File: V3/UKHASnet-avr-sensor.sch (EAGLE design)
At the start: 25 parts, among them J1 AVR_SPI_PRG_62X3_LOCK, U1 MCP1700-3302E/TO, U2 ATMEGA328P-PU, X2 SMA-142-0711-821/826, Y1 RESONATORPTH

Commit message: Add final V3 files.
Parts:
- removed JP1: M02PTH, SparkFun-Connectors:M02PTH
- added JP7: M02JST-PTH-VERT, SparkFun-Connectors:M02JST-PTH-VERT
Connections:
- net GND: now also JP6.1, JP6.2, JP7.1; no longer JP1.1, JP6.3, JP6.4
- net SENSE1: now also JP6.3; no longer JP6.2
- net SENSE_VCC: now also JP6.4; no longer JP6.1
- net VIN: now also JP7.2; no longer JP1.2
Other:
- moved on the sheet: JP6
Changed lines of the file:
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@@
 <part name="U$1" library="hopeRF2" deviceset="RFM69HW" device=""/>
 <part name="J1" library="SparkFun-Connectors" deviceset="AVR_SPI_PRG_6" device="2X3_LOCK"/>
-<part name="JP1" library="SparkFun-Connectors" deviceset="M02" device="PTH"/>
 <part name="JP2" library="SparkFun-Connectors" deviceset="M01" device="PTH"/>
 <part name="JP3" library="SparkFun-Connectors" deviceset="M01" device="PTH"/>
@@
 <part name="X2" library="con-coax" deviceset="SMA-" device="142-0711-821/826"/>
 <part name="JP6" library="SparkFun-Connectors" deviceset="M04" device="PTH"/>
+<part name="JP7" library="SparkFun-Connectors" deviceset="M02" device="JST-PTH-VERT"/>
 </parts>
 <sheets>
@@
 <instance part="U$1" gate="A" x="25.4" y="-22.86" rot="R180"/>
 <instance part="J1" gate="G$1" x="104.14" y="104.14"/>
-<instance part="JP1" gate="G$1" x="-68.58" y="101.6"/>
 <instance part="JP2" gate="G$1" x="-68.58" y="86.36"/>
 <instance part="JP3" gate="G$1" x="-68.58" y="73.66"/>
@@
 <instance part="JP5" gate="G$1" x="147.32" y="15.24" rot="R180"/>
 <instance part="X2" gate="G1" x="96.52" y="-5.08" rot="MR0"/>
-<instance part="JP6" gate="G$1" x="-33.02" y="55.88" rot="MR180"/>
+<instance part="JP6" gate="G$1" x="-33.02" y="53.34"/>
+<instance part="JP7" gate="G$1" x="-76.2" y="104.14" rot="MR180"/>
 </instances>
 <busses>
@@
 <segment>
 <pinref part="R4" gate="G$1" pin="1"/>
+<wire x1="-17.78" y1="55.88" x2="10.16" y2="55.88" width="0.1524" layer="91"/>
+<label x="0" y="55.88" size="1.778" layer="95"/>
+<pinref part="JP6" gate="G$1" pin="3"/>
 <wire x1="-27.94" y1="55.88" x2="-17.78" y2="55.88" width="0.1524" layer="91"/>
-<wire x1="-17.78" y1="55.88" x2="10.16" y2="55.88" width="0.1524" layer="91"/>
 <junction x="-17.78" y="55.88"/>
-<label x="0" y="55.88" size="1.778" layer="95"/>
-<pinref part="JP6" gate="G$1" pin="2"/>
 </segment>
 </net>
@@
 <wire x1="-55.88" y1="86.36" x2="-53.34" y2="86.36" width="0.1524" layer="91"/>
 <junction x="-55.88" y="86.36"/>
-<pinref part="JP1" gate="G$1" pin="1"/>
 <wire x1="-60.96" y1="101.6" x2="-60.96" y2="91.44" width="0.1524" layer="91"/>
 <wire x1="-60.96" y1="91.44" x2="-53.34" y2="91.44" width="0.1524" layer="91"/>
@@
 <wire x1="15.24" y1="93.98" x2="15.24" y2="91.44" width="0.1524" layer="91"/>
 <junction x="15.24" y="91.44"/>
+<wire x1="-60.96" y1="101.6" x2="-63.5" y2="101.6" width="0.1524" layer="91"/>
+<wire x1="-63.5" y1="101.6" x2="-66.04" y2="104.14" width="0.1524" layer="91"/>
+<pinref part="JP7" gate="G$1" pin="1"/>
+<wire x1="-66.04" y1="104.14" x2="-68.58" y2="104.14" width="0.1524" layer="91"/>
 </segment>
 <segment>
@@
 <segment>
 <label x="-10.16" y="53.34" size="1.778" layer="95"/>
-<wire x1="-27.94" y1="53.34" x2="-25.4" y2="53.34" width="0.1524" layer="91"/>
 <pinref part="C7" gate="G$1" pin="2"/>
 <wire x1="-25.4" y1="53.34" x2="-10.16" y2="53.34" width="0.1524" layer="91"/>
 <wire x1="-10.16" y1="55.88" x2="-10.16" y2="53.34" width="0.1524" layer="91"/>
-<pinref part="JP6" gate="G$1" pin="3"/>
-<pinref part="JP6" gate="G$1" pin="4"/>
-<wire x1="-27.94" y1="50.8" x2="-25.4" y2="50.8" width="0.1524" layer="91"/>
 <wire x1="-25.4" y1="50.8" x2="-25.4" y2="53.34" width="0.1524" layer="91"/>
+<pinref part="JP6" gate="G$1" pin="2"/>
+<wire x1="-27.94" y1="53.34" x2="-25.4" y2="53.34" width="0.1524" layer="91"/>
 <junction x="-25.4" y="53.34"/>
+<pinref part="JP6" gate="G$1" pin="1"/>
+<wire x1="-25.4" y1="50.8" x2="-27.94" y2="50.8" width="0.1524" layer="91"/>
 </segment>
 <segment>
@@
 <segment>
 <pinref part="U1" gate="A" pin="VIN"/>
-<pinref part="JP1" gate="G$1" pin="2"/>
 <wire x1="-40.64" y1="104.14" x2="-50.8" y2="104.14" width="0.1524" layer="91"/>
 <label x="-58.42" y="104.14" size="1.778" layer="95"/>
 <pinref part="C4" gate="G$1" pin="1"/>
-<wire x1="-50.8" y1="104.14" x2="-60.96" y2="104.14" width="0.1524" layer="91"/>
 <wire x1="-50.8" y1="101.6" x2="-50.8" y2="104.14" width="0.1524" layer="91"/>
+<wire x1="-50.8" y1="104.14" x2="-63.5" y2="104.14" width="0.1524" layer="91"/>
 <junction x="-50.8" y="104.14"/>
+<wire x1="-63.5" y1="104.14" x2="-66.04" y2="101.6" width="0.1524" layer="91"/>
+<pinref part="JP7" gate="G$1" pin="2"/>
+<wire x1="-66.04" y1="101.6" x2="-68.58" y2="101.6" width="0.1524" layer="91"/>
 </segment>
 <segment>
@@
 <pinref part="C7" gate="G$1" pin="1"/>
 <wire x1="-10.16" y1="63.5" x2="-10.16" y2="66.04" width="0.1524" layer="91"/>
-<pinref part="JP6" gate="G$1" pin="1"/>
+<pinref part="JP6" gate="G$1" pin="4"/>
 <wire x1="-27.94" y1="58.42" x2="-22.86" y2="58.42" width="0.1524" layer="91"/>
 </segment>

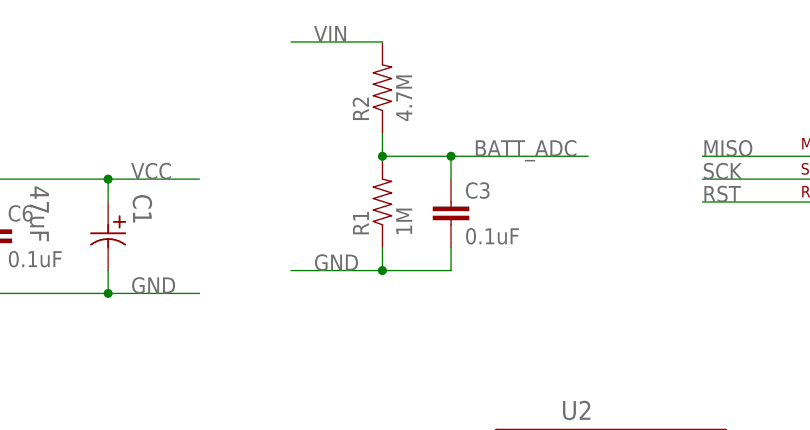
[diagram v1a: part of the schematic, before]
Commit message: Reduce Battery Voltage Resistor Divider Values.
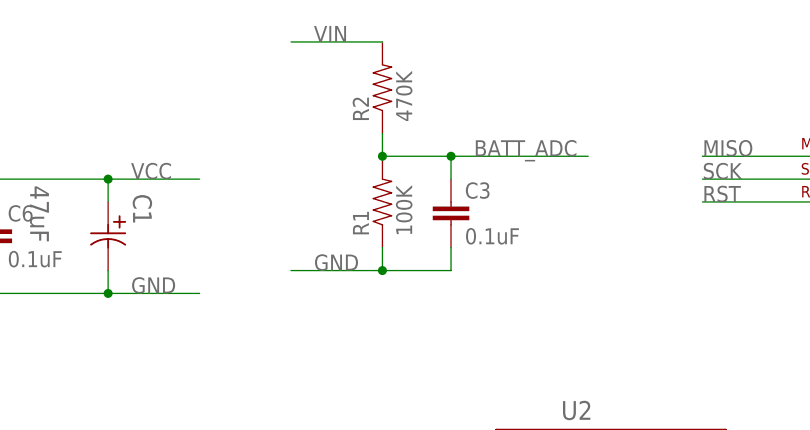
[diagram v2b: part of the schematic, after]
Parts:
- R1: value 1M -> 100K
- R2: value 4.7M -> 470K
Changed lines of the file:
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@@
 <part name="U1" library="mcp1700" deviceset="MCP1700-3302E/TO" device=""/>
 <part name="JP9" library="SparkFun-Connectors" deviceset="M01" device="PTH"/>
-<part name="R1" library="SparkFun" deviceset="RESISTOR" device="PTH-1/4W" value="1M"/>
-<part name="R2" library="SparkFun" deviceset="RESISTOR" device="PTH-1/4W" value="4.7M"/>
+<part name="R1" library="SparkFun" deviceset="RESISTOR" device="PTH-1/4W" value="100K"/>
+<part name="R2" library="SparkFun" deviceset="RESISTOR" device="PTH-1/4W" value="470K"/>
 <part name="R3" library="SparkFun" deviceset="RESISTOR" device="PTH-1/4W" value="10K"/>
 <part name="C1" library="1000ufCap" deviceset="EEU" device="-P1.5" technology="FC1J6R8" value="47uF"/>
